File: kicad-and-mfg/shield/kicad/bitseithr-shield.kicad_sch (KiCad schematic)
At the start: 60 parts, among them CN1 SHIELD CONN 2, CN10 SHIELD CONN 3, CN11 SHIELD CONN 4, CN12 SHIELD CONN 5, CN2 SHIELD CONN 7, CN3 SHIELD CONN 8, CN4 PIGTAIL 4, CN5 PIGTAIL 3, CN6 PIGTAIL 5, CN7 PIGTAIL 1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

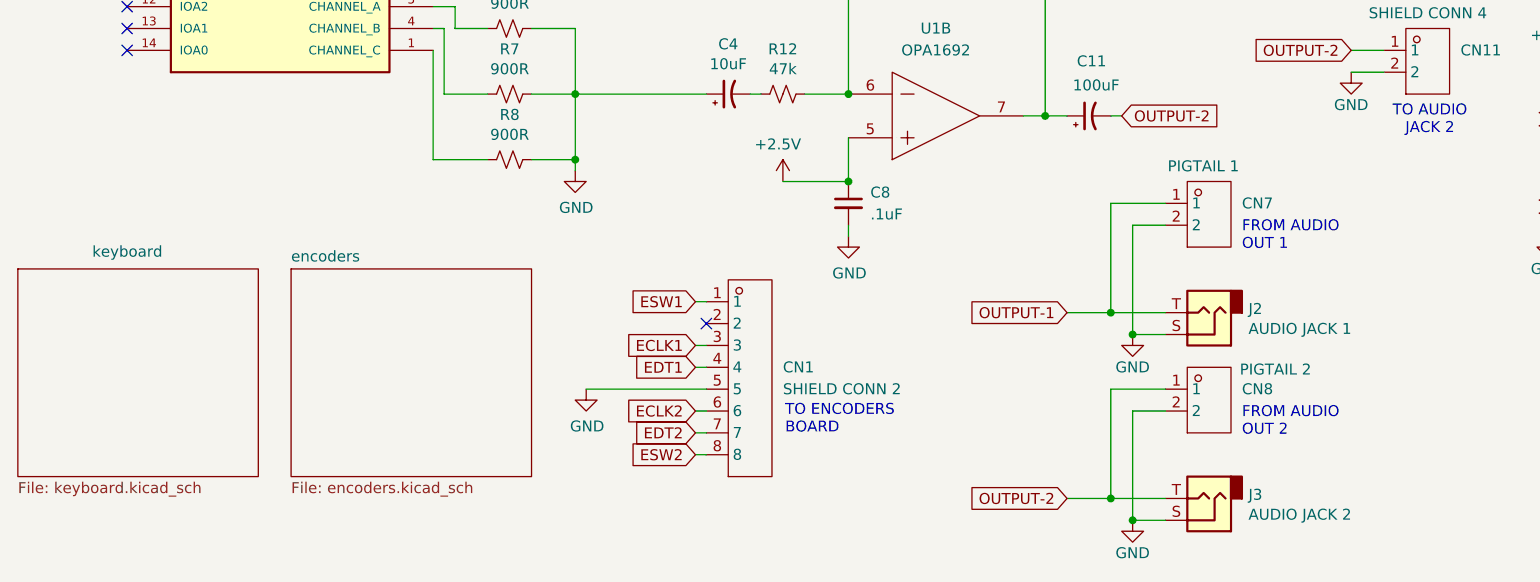
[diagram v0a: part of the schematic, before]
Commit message: moved keyboard pcb 1.5mm left, started shield schematic
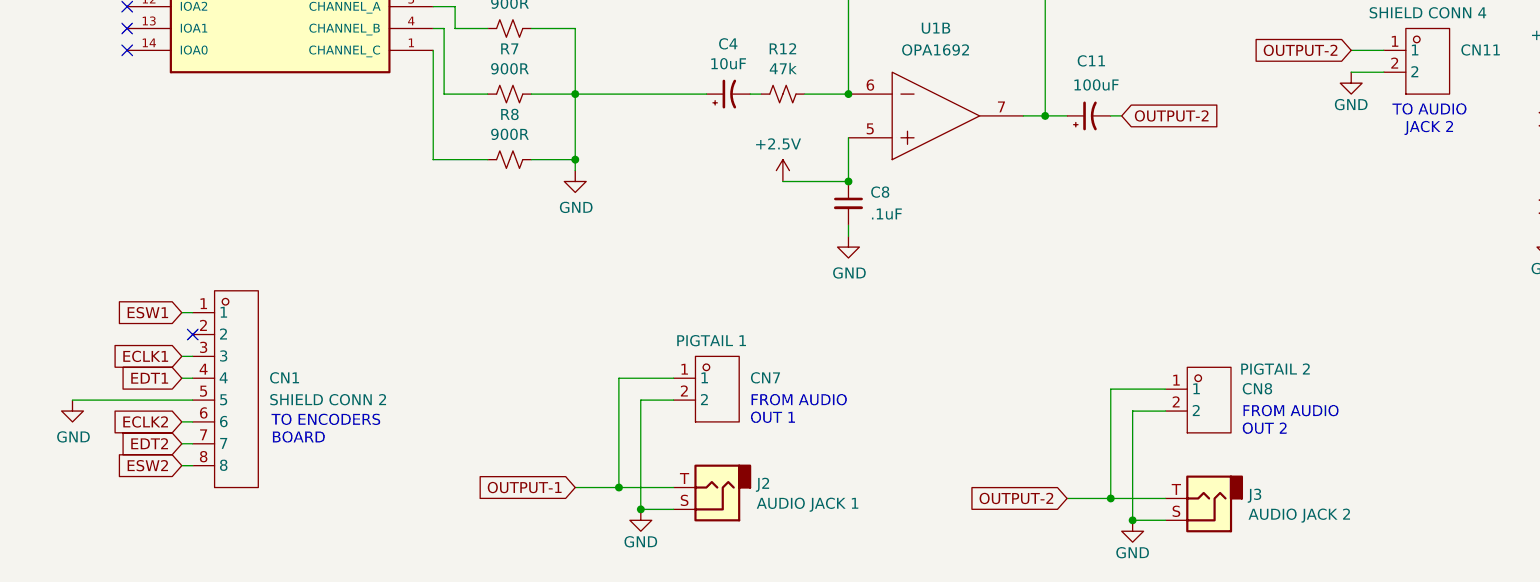
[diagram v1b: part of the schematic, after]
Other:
- removed sheet encoders
- removed sheet keyboard
- moved on the sheet: CN1, CN7, J2

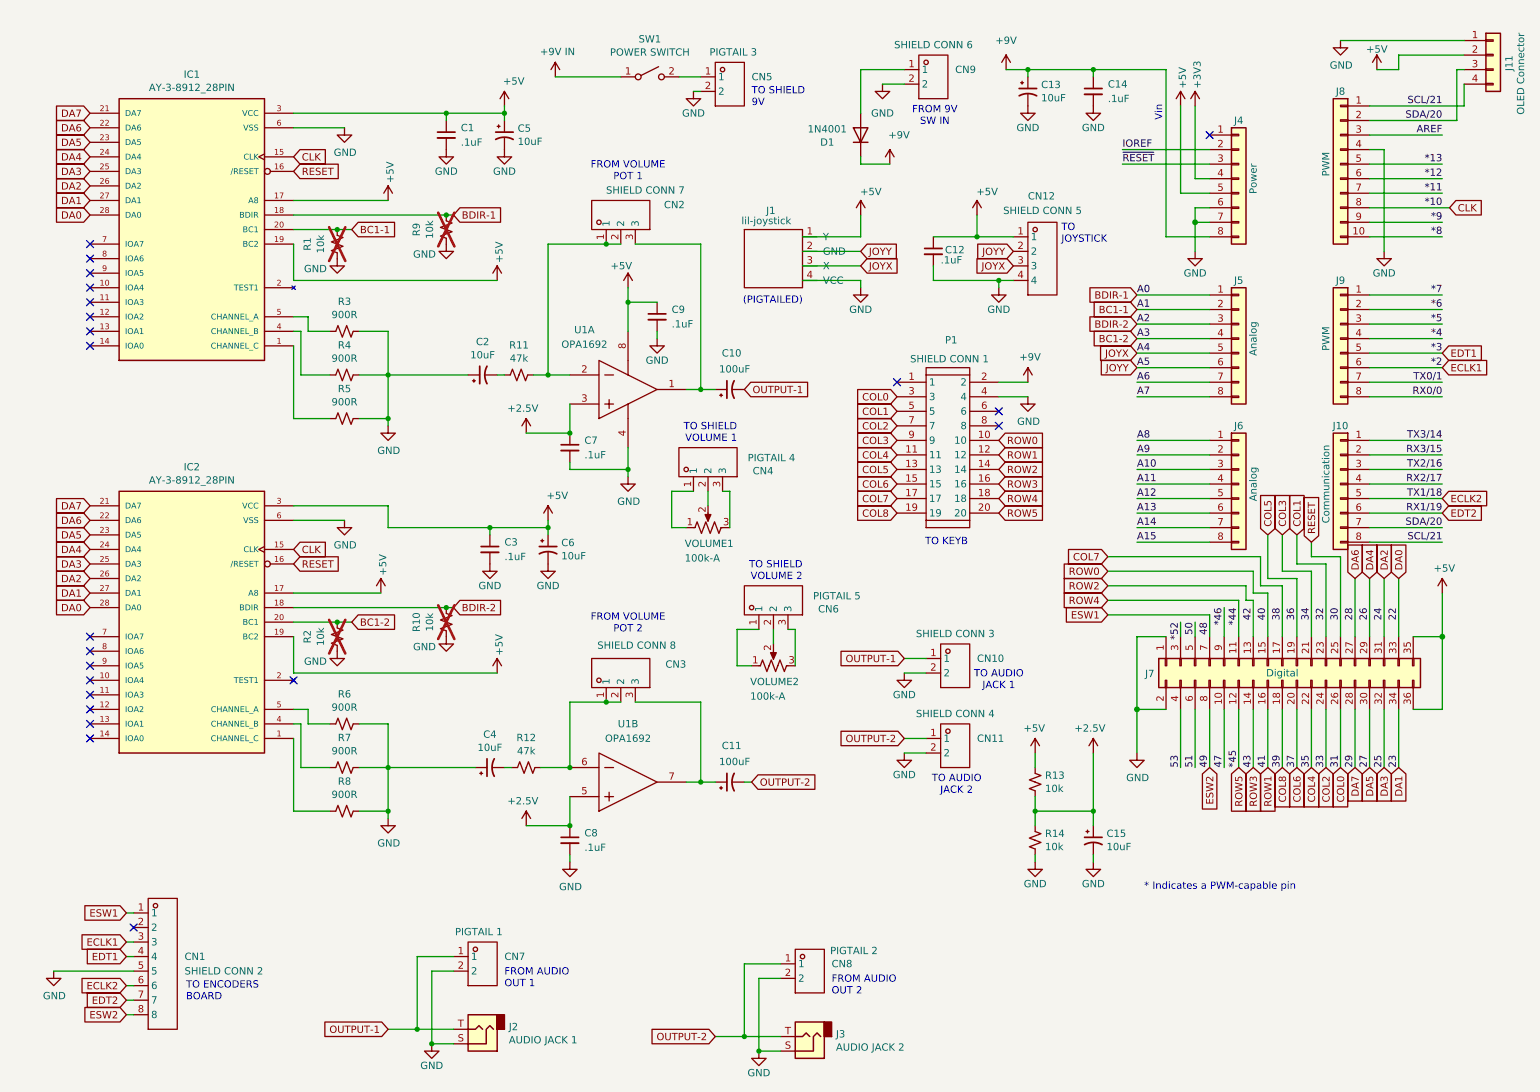
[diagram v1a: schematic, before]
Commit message: shield schematic cleanup. fixed sound output section (using op amps as inverting summer now too)
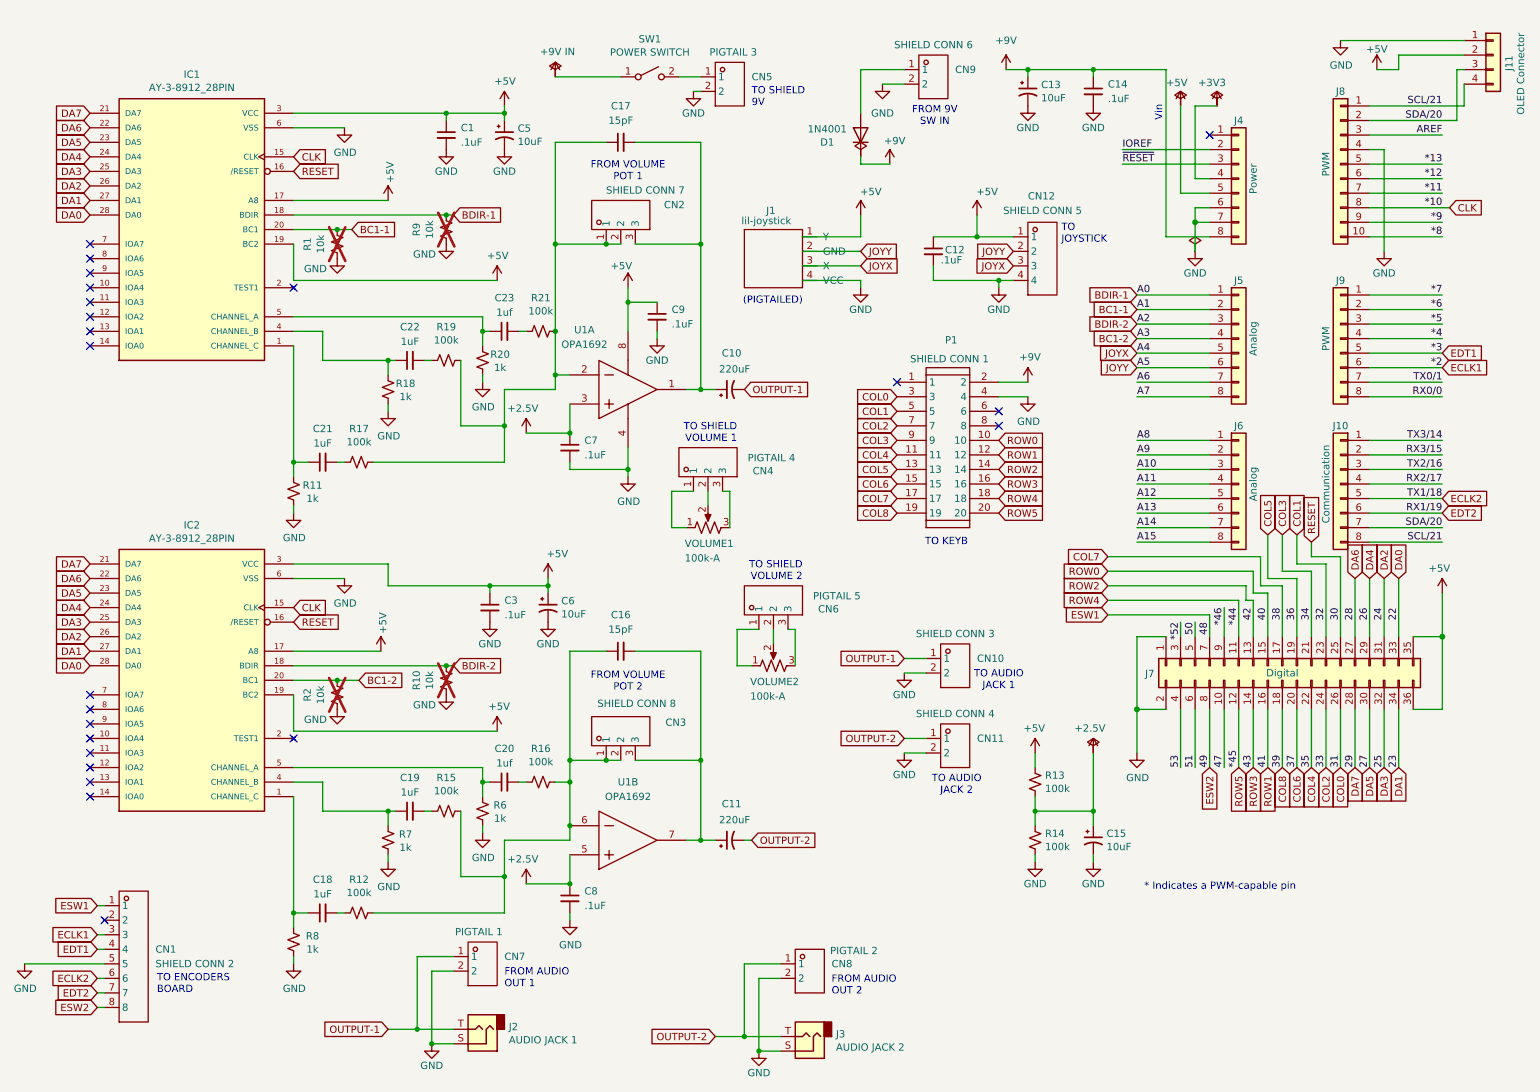
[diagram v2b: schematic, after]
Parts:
- removed C2, C4: 10uF, cholm-footprints:0801, symbol Device:C_Polarized_Small_US
- removed R3, R4, R5: 900R, symbol Device:R_Small_US
- added C16, C17: 15pF, Capacitor_SMD:C_0603_1608Metric_Pad1.08x0.95mm_HandSolder, symbol Device:C_Small
- added C18, C19, C21, C22: 1uF, symbol Device:C_Small
- added C20, C23: 1uf, symbol Device:C_Small
- added R15, R16, R17, R19, R21: 100k, Resistor_SMD:R_1206_3216Metric, symbol Device:R_Small_US
- added R18, R20: 1k, symbol Device:R_Small_US
- C10, C11: value 100uF -> 220uF
- CN1: symbol EasyEDA_Lib:HC-XA-8AW -> bitseithr-shield:HC-XA-8AW
- CN10, CN11, CN5, CN7, CN8, CN9: symbol EasyEDA_Lib:HC-XA-2AW -> bitseithr-shield:HC-XA-2AW
- CN12: symbol EasyEDA_Lib:HC-XA-4AW -> bitseithr-shield:HC-XA-4AW
- CN2, CN3, CN4, CN6: symbol EasyEDA_Lib:HC-XA-3AW -> bitseithr-shield:HC-XA-3AW
- P1: symbol EasyEDA_Lib:IDC Box 2X10 2.54MM -> bitseithr-shield:IDC Box 2X10 2.54MM
- R11: value 47k -> 1k; footprint Resistor_SMD:R_1206_3216Metric -> (none)
- R12: value 47k -> 100k
- R13, R14: value 10k -> 100k
- R6, R7, R8: value 900R -> 1k
- U1: symbol EasyEDA_Lib:OPA1692IDR -> bitseithr-shield:OPA1692IDR
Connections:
- net GND: now also R11.1, R18.1, R20.1
- net at IC1.1 (CHANNEL_C): now also R11.2, C21.1
- net at IC1.4 (CHANNEL_B): now also C22.1, R18.2
- net at IC1.5 (CHANNEL_A): now also C23.1, R20.2
- net at CN3.1, CN3.2, R12.1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: now also C16.1, R15.1, R16.1
- net at C11.1, CN3.3, U1.7 (OUT2): now also C16.2
- net at C10.1, CN2.3, U1.1 (OUT1): now also C17.2
- net at CN2.1, CN2.2, U1.2 (IN1-): now also C17.1, R17.1, R19.1, R21.1; no longer R11.1
- net at IC2.1 (CHANNEL_C), R8.2: now also C18.1
- net at IC2.4 (CHANNEL_B), R7.2: now also C19.1
- net at IC2.5 (CHANNEL_A), R6.2: now also C20.1
- net at R12.2: now also C18.2
- new net: C22.2, R19.2
- new net: C20.2, R16.2
- new net: C23.2, R21.2
- new net: C19.2, R15.2
- new net: C21.2, R17.2
- no-connect marks 22 -> 23
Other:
- moved on the sheet: C11, C3, C6, C8, CN1, CN3, IC2, R10, R12, R2, R6, R7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

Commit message: fixed some naming issues
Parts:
- C20, C23: value 1uf -> 1uF
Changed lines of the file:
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@@
 	)
 	(junction
+		(at 114.3 66.04)
+		(diameter 0)
+		(color 0 0 0 0)
+	)
+	(junction
 		(at 115.57 140.97)
 		(diameter 0)
@@
 	)
 	(junction
-		(at 113.03 50.8)
+		(at 114.3 73.66)
 		(diameter 0)
 		(color 0 0 0 0)
@@
 	)
 	(junction
-		(at 207.01 149.86)
+		(at 114.3 50.8)
 		(diameter 0)
 		(color 0 0 0 0)
 	)
 	(junction
-		(at 100.33 144.78)
+		(at 207.01 149.86)
 		(diameter 0)
 		(color 0 0 0 0)
 	)
 	(junction
-		(at 74.93 48.26)
+		(at 100.33 144.78)
 		(diameter 0)
 		(color 0 0 0 0)
 	)
 	(junction
-		(at 146.05 189.23)
+		(at 74.93 48.26)
 		(diameter 0)
 		(color 0 0 0 0)
 	)
 	(junction
-		(at 113.03 73.66)
+		(at 146.05 189.23)
 		(diameter 0)
 		(color 0 0 0 0)
@@
 	)
 	(junction
-		(at 113.03 66.04)
-		(diameter 0)
-		(color 0 0 0 0)
-	)
-	(junction
 		(at 100.33 66.04)
 		(diameter 0)
@@
 	(wire
 		(pts
-			(xy 113.03 33.02) (xy 121.92 33.02)
+			(xy 114.3 33.02) (xy 121.92 33.02)
 		)
 		(stroke
@@
 	(wire
 		(pts
+			(xy 114.3 73.66) (xy 115.57 73.66)
+		)
+		(stroke
+			(width 0)
+			(type default)
+		)
+	)
+	(wire
+		(pts
 			(xy 242.57 132.08) (xy 242.57 142.24)
 		)
@@
 	(wire
 		(pts
+			(xy 114.3 50.8) (xy 121.92 50.8)
+		)
+		(stroke
+			(width 0)
+			(type default)
+		)
+	)
+	(wire
+		(pts
 			(xy 83.82 106.68) (xy 83.82 110.49)
 		)
@@
 	(wire
 		(pts
-			(xy 113.03 73.66) (xy 115.57 73.66)
-		)
-		(stroke
-			(width 0)
-			(type default)
-		)
-	)
-	(wire
-		(pts
 			(xy 214.63 102.87) (xy 227.33 102.87)
 		)
@@
 	(wire
 		(pts
-			(xy 113.03 50.8) (xy 113.03 33.02)
+			(xy 114.3 50.8) (xy 114.3 33.02)
 		)
 		(stroke
@@
 	(wire
 		(pts
-			(xy 113.03 73.66) (xy 113.03 76.2)
-		)
-		(stroke
-			(width 0)
-			(type default)
-		)
-	)
-	(wire
-		(pts
 			(xy 271.78 22.86) (xy 271.78 26.67)
 		)
@@
 	(wire
 		(pts
-			(xy 113.03 50.8) (xy 113.03 66.04)
+			(xy 114.3 50.8) (xy 114.3 66.04)
 		)
 		(stroke
@@
 	(wire
 		(pts
-			(xy 104.14 76.2) (xy 113.03 76.2)
+			(xy 104.14 76.2) (xy 114.3 76.2)
 		)
 		(stroke
@@
 	(wire
 		(pts
-			(xy 113.03 66.04) (xy 113.03 73.66)
+			(xy 114.3 66.04) (xy 114.3 73.66)
 		)
 		(stroke
@@
 	(wire
 		(pts
-			(xy 113.03 50.8) (xy 121.92 50.8)
-		)
-		(stroke
-			(width 0)
-			(type default)
-		)
-	)
-	(wire
-		(pts
 			(xy 227.33 115.57) (xy 227.33 119.38)
 		)
@@
 	(wire
 		(pts
+			(xy 114.3 66.04) (xy 113.03 66.04)
+		)
+		(stroke
+			(width 0)
+			(type default)
+		)
+	)
+	(wire
+		(pts
 			(xy 104.14 27.94) (xy 104.14 26.67)
 		)
@@
 	(wire
 		(pts
+			(xy 114.3 76.2) (xy 114.3 73.66)
+		)
+		(stroke
+			(width 0)
+			(type default)
+		)
+	)
+	(wire
+		(pts
 			(xy 227.33 69.85) (xy 214.63 69.85)
 		)
@@
 		(dnp no)
 		(property "Reference" "U1"
-			(at 118.11 65.786 0)
+			(at 119.634 64.008 0)
 			(show_name no)
 			(do_not_autoplace no)
@@
 		)
 		(property "Value" "OPA1692"
-			(at 118.11 68.326 0)
+			(at 119.634 66.548 0)
 			(show_name no)
 			(do_not_autoplace no)
@@
 			)
 		)
-		(property "Value" "1uf"
+		(property "Value" "1uF"
 			(at 104.14 62.738 90)
 			(show_name no)
@@
 			)
 		)
-		(property "Value" "1uf"
+		(property "Value" "1uF"
 			(at 104.14 141.478 90)
 			(show_name no)
